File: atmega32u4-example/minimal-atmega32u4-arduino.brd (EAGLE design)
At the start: 36.8 x 41.9 mm, 32 parts, among them U1 MCP73831, U2 MIC5219, U3 32U4, X1 USB-MICROB, Y1 8MHz

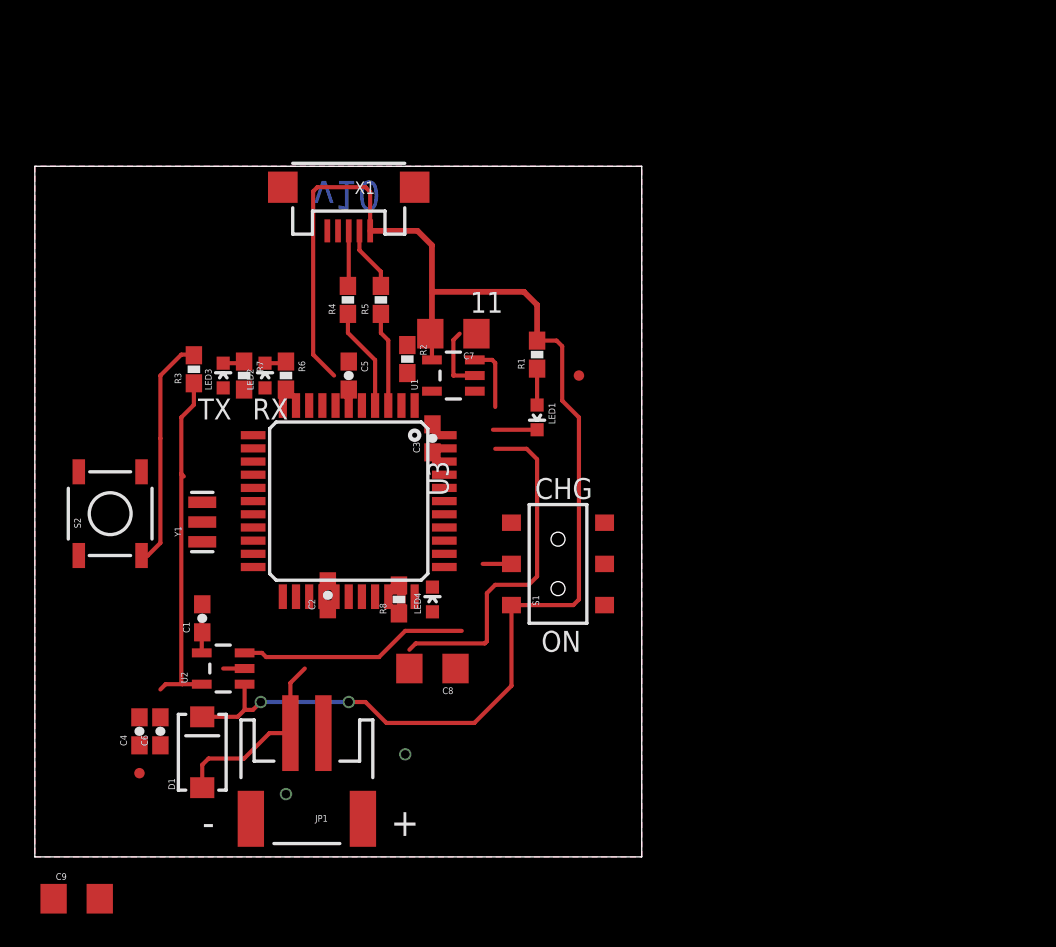
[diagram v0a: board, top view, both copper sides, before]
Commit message: Finished layout and BOM of ATMEGA32u4 board. Uses mostly the same parts as the 328 board now.
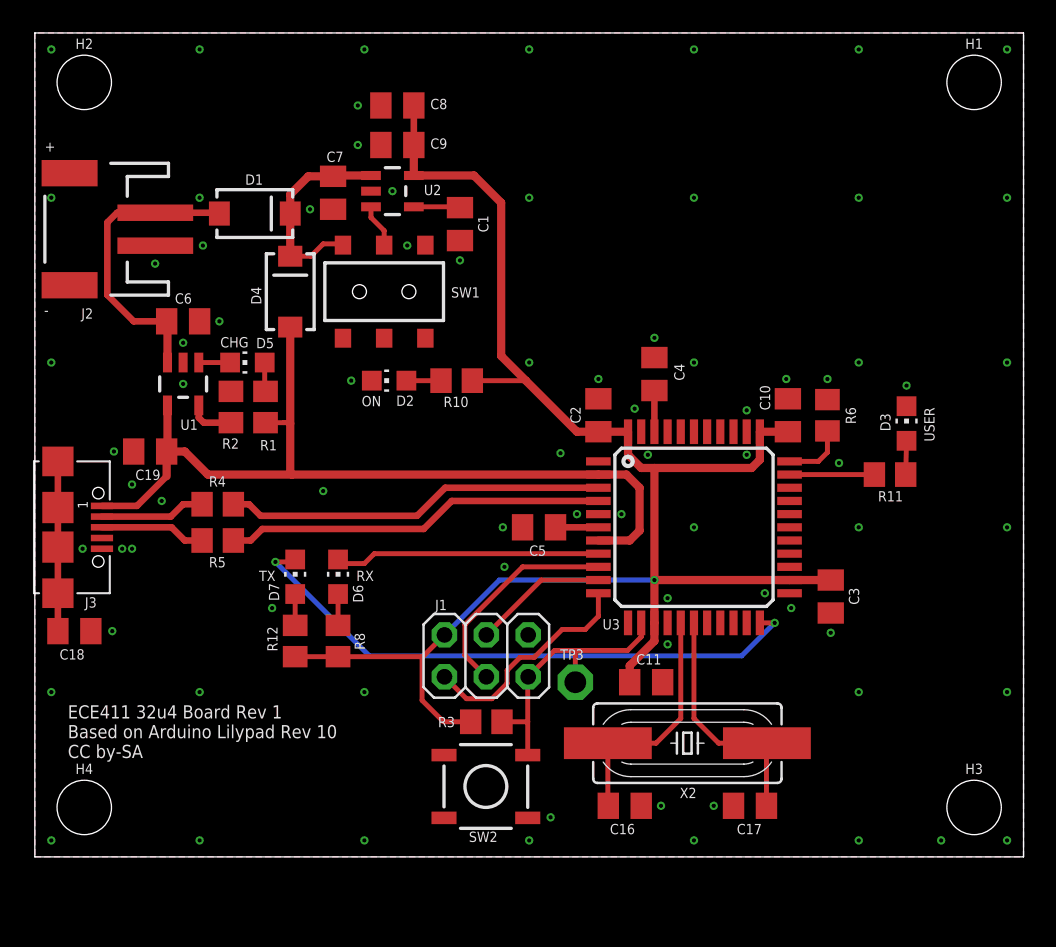
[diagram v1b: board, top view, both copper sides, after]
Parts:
- removed JP1: JST-2, SparkFun-Connectors:JST-2-SMD
- removed JP2, JP3: FIDUCIALUFIDUCIAL, SparkFun:MICRO-FIDUCIAL
- removed LED1, LED2, LED3, LED4: RED, SparkFun-LED:LED-0603
- removed R7: 330, SparkFun-Passives:0603-RES
- removed S1: SWITCH-DPDTSMD, SparkFun-Electromechanical:AYZ0202
- removed S2: !RESET, SparkFun-Electromechanical:TACTILE_SWITCH_SMD
- removed X1: USB-MICROB, SparkFun-Connectors:USB-MICROB
- removed Y1: 8MHz, SparkFun-FreqCtrl:RESONATOR-SMD
- added C10, C11, C18: 100n, rcl:C0805K
- added C16, C17: 18p, rcl:C0805K
- added C19: 4.7u, rcl:C0805K
- added D2, D3, D5, D6, D7: GREEN, led:CHIP-LED0805
- added D4: B340A, SparkFun-DiscreteSemi:SMA-DIODE
- added H1, H2, H3, H4: STAND-OFF, SparkFun-Hardware:STAND-OFF
- added J1: 3x2 M, SmartPrj:2X03
- added J2: S2B-PH-SM4-TB(LF)(SN), SparkFun-Connectors:JST-2-SMD
- added J3: 629105136821, Wurth_Elektronik_Electromechanic_Input-Output_Connectors_rev19b:629105136821
- added R10, R11, R12: 1K, rcl:R0805
- added SW1: AYZ0202AGRLC, SparkFun-Electromechanical:AYZ0202
- added SW2: !RESET, SparkFun-Electromechanical:TACTILE_SWITCH_SMD
- added TP3: TPPAD1-13, testpad:P1-13
- added X2: 16 MHz, SparkFun-Clocks:HC49UP
- C1: value 470pF -> 470p; device SparkFun-Passives:0603-CAP -> rcl:C0805K
- C2, C3, C4: value .1uF -> 100n; device SparkFun-Passives:0603-CAP -> rcl:C0805K
- C5: value 1uF -> 1u; device SparkFun-Passives:0603-CAP -> rcl:C0805K
- C6: value 4.7uF -> 4.7u; device SparkFun-Passives:0603-CAP -> rcl:C0805K
- C7, C8: value 4.7uF -> 4.7u; device SparkFun-Passives:1206 -> rcl:C0805K
- C9: value 4.7uF -> 100n; device SparkFun-Passives:1206 -> rcl:C0805K
- R1, R8: value 330 -> 1K; device SparkFun-Passives:0603-RES -> rcl:R0805
- R2, R3: value 10k -> 10K; device SparkFun-Passives:0603-RES -> rcl:R0805
- R4, R5: device SparkFun-Passives:0603-RES -> rcl:R0805
- R6: value 330 -> 10K; device SparkFun-Passives:0603-RES -> rcl:R0805
- U3: value 32U4 -> ATMEGA32U4-AUR
- moved C9 49.7 mm to (22.0, 43.2), turned to 180 degrees
- moved C4 38.0 mm to (37.6, 29.3)
- moved C8 34.2 mm to (22.0, 45.6)
- moved R6 32.9 mm to (48.1, 26.8)
- moved D1 32.8 mm to (13.4, 39.0), turned to 0 degrees
- moved U2 30.7 mm to (21.7, 40.4), turned to 270 degrees
- moved C1 28.6 mm to (25.8, 38.4), turned to 270 degrees
- moved R3 27.8 mm to (27.4, 8.20), turned to 180 degrees
- moved C3 26.0 mm to (48.3, 15.8), turned to 270 degrees
- moved C6 24.9 mm to (9.00, 32.5), turned to 0 degrees
- moved U3 21.0 mm to (40.0, 20.0), turned to 0 degrees
- moved C2 19.7 mm to (34.2, 26.8)
- moved R5 17.6 mm to (11.1, 19.2), turned to 0 degrees
- moved R1 16.8 mm to (14.0, 27.3), turned to 270 degrees
- moved U1 16.4 mm to (9.00, 28.7), turned to 180 degrees
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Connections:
- net N$6 renamed MCPPROG
- net N$8 renamed MIC-BP
- removed net 5V: C7.2, C9.2, D1.C, R1.2, S1.1, U1.4, U2.1, U3.7, X1.VBUS
- removed net MISO: U3.11
- removed net MOSI: U3.10
- removed net N$1: LED2.C, R6.1
- removed net N$18: LED4.A, R8.1
- removed net N$2: S1.2, U2.3
- removed net N$21: LED3.C, R7.1
- removed net N$5: U3.17, Y1.1
- removed net RESET: R3.2, S2.3, U3.13
- removed net RX_LED: R6.2, U3.8
- removed net SCK: U3.9
- removed net USER_LED: R8.2, U3.32
- new net !RESET: J1.5, R3.1, SW2.3, TP3.TP, U3.13
- new net AREF: C4.1, U3.42
- new net D13#/USER_LED: R11.2, U3.32
- new net D14/MISO: J1.1, U3.11
- new net D15/SCK: J1.3, U3.9
- new net D16/MOSI: J1.4, U3.10
- new net D17/RX-LED: D6.C, U3.8
- new net MIC-EN: SW1.2, U2.3
- new net N$13: D3.A, R11.1
- new net N$14: C18.1, J3.SHELL, J3.SHELL1, J3.SHELL2, J3.SHELL3
- new net N$15: D6.A, R8.1
- new net N$16: D7.A, R12.1
- new net PE2/!HWB: R6.2, U3.33
- new net PWRIN: C7.1, D1.C, D4.C, SW1.1, U2.1
- new net UCAP: C5.1, U3.6
- new net VBUS: C19.1, D4.A, J3.1, R1.2, U1.4, U3.2, U3.7
- new net XTAL1: C17.1, U3.17, X2.2
- new net XTAL2: C16.1, U3.16, X2.1
- net 3.3V: now also C10.1, C11.1, C2.1, C3.1, C8.1, C9.1, J1.2, R10.2, R12.2, R3.2, R8.2; no longer C2.2, C3.2, C4.2, C5.2, C6.2, LED2.A, LED3.A, R3.1, U3.42, U3.6
- net D+: now also R5.2; no longer R4.1
- net D-: now also R4.2; no longer R5.1
- net GND: now also C10.2, C11.2, C16.2, C17.2, C18.2, C19.2, C2.2, C3.2, C4.2, C5.2, C6.2, C7.2, C8.2, C9.2, D2.C, D3.C, J1.6, J2.1, J3.5, R6.1, SW1.3, SW2.1; no longer C2.1, C3.1, C4.1, C5.1, C6.1, C7.1, C8.1, C9.1, JP1.1, LED4.C, S1.3, S2.1, U3.33, X1.GND, X1.MT1, X1.MT2, Y1.2
- net N$19: now also J3.2, R4.1; no longer R5.2, X1.D-
- net N$20: now also J3.3, R5.1; no longer R4.2, X1.D+
- net N$3: now also D5.A; no longer LED1.A
- net N$4: now also D5.C; no longer LED1.C
- net N$7: now also D2.A, R10.1; no longer U3.16, Y1.3
- net TX_LED: now also D7.C; no longer R7.2
- net V_BATT: now also C6.1, J2.2; no longer C8.2, JP1.2
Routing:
- net 5V: track 86.4 -> 0.00 mm, vias 2 -> 0
- net 3.3V: track 21.7 -> 99.9 mm, vias 0 -> 1
- net VBUS: track 0.00 -> 54.7 mm
- net TX_LED: track 0.00 -> 35.7 mm, vias 0 -> 2
- net V_BATT: track 37.0 -> 18.2 mm
- net D-: track 5.75 -> 23.1 mm
- net !RESET: track 0.00 -> 17.0 mm
- net D+: track 6.24 -> 23.1 mm
- net D17/RX-LED: track 0.00 -> 16.2 mm
- net N$2: track 15.7 -> 0.00 mm
- net XTAL1: track 0.00 -> 14.7 mm
- net XTAL2: track 0.00 -> 14.7 mm
- net RESET: track 14.2 -> 0.00 mm
- net D14/MISO: track 0.00 -> 13.8 mm
- net D15/SCK: track 0.00 -> 13.3 mm
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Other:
- board size 36.8 x 41.9 mm -> 60 x 50 mm
- board text added: "ECE411 32u4 Board Rev 1 Based on Arduino Lilypad Rev 10 CC by-SA"
- board text added: "USER"
- board text removed: "11"
- board text removed: "v10"

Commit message: Eeek! Bad cap values for the crystal oscillator. Changed from 18pF to 30 pF based on 18 pF load cap and 0805 capacitors.
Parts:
- C16, C17: value 18p -> 30p
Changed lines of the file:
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@@
 <attribute name="VALUE" x="39.6" y="4.233" size="0.6096" layer="27" font="vector" ratio="20" align="top-center"/>
 </element>
-<element name="C16" library="rcl" library_urn="urn:adsk.eagle:library:334" package="C0805K" package3d_urn="urn:adsk.eagle:package:23681/2" value="18p" x="35.8" y="3.1" smashed="yes">
-<attribute name="DESC" value="CAP CER 18PF 50V C0G/NP0 0805" x="35.8" y="3.1" size="1.778" layer="27" display="off"/>
+<element name="C16" library="rcl" library_urn="urn:adsk.eagle:library:334" package="C0805K" package3d_urn="urn:adsk.eagle:package:23681/2" value="30p" x="35.8" y="3.1" smashed="yes">
+<attribute name="DESC" value="CAP CER 30PF 50V C0G/NP0 0805" x="35.8" y="3.1" size="1.778" layer="27" display="off"/>
 <attribute name="MFR" value="Samsung" x="-5" y="-37.7" size="1.778" layer="27" display="off"/>
-<attribute name="MPN" value="CL21C180JBANNNC" x="-5" y="-37.7" size="1.778" layer="27" display="off"/>
+<attribute name="MPN" value="CL21C300JBANNNC" x="-5" y="-37.7" size="1.778" layer="27" display="off"/>
 <attribute name="NAME" x="34.9" y="1.375" size="0.625" layer="25" font="vector" ratio="20"/>
 <attribute name="POPULARITY" value="52" x="-5" y="-37.7" size="1.778" layer="27" display="off"/>
@@
 <attribute name="VALUE" x="34.8" y="1.2" size="1.016" layer="27"/>
 </element>
-<element name="C17" library="rcl" library_urn="urn:adsk.eagle:library:334" package="C0805K" package3d_urn="urn:adsk.eagle:package:23681/2" value="18p" x="43.4" y="3.1" smashed="yes" rot="R180">
-<attribute name="DESC" value="CAP CER 18PF 50V C0G/NP0 0805" x="43.4" y="3.1" size="1.778" layer="27" rot="R180" display="off"/>
+<element name="C17" library="rcl" library_urn="urn:adsk.eagle:library:334" package="C0805K" package3d_urn="urn:adsk.eagle:package:23681/2" value="30p" x="43.4" y="3.1" smashed="yes" rot="R180">
+<attribute name="DESC" value="CAP CER 30PF 50V C0G/NP0 0805" x="43.4" y="3.1" size="1.778" layer="27" rot="R180" display="off"/>
 <attribute name="MFR" value="Samsung" x="88" y="48.7" size="1.778" layer="27" rot="R180" display="off"/>
 <attribute name="MPN" value="CL21C180JBANNNC" x="88" y="48.7" size="1.778" layer="27" rot="R180" display="off"/>
